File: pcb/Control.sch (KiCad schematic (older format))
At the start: 26 parts, among them P201 USB_OTG, P202 CONN_01X04, P203 CONN_01X04, U201 AP2114H, U202 STM32F072CBU

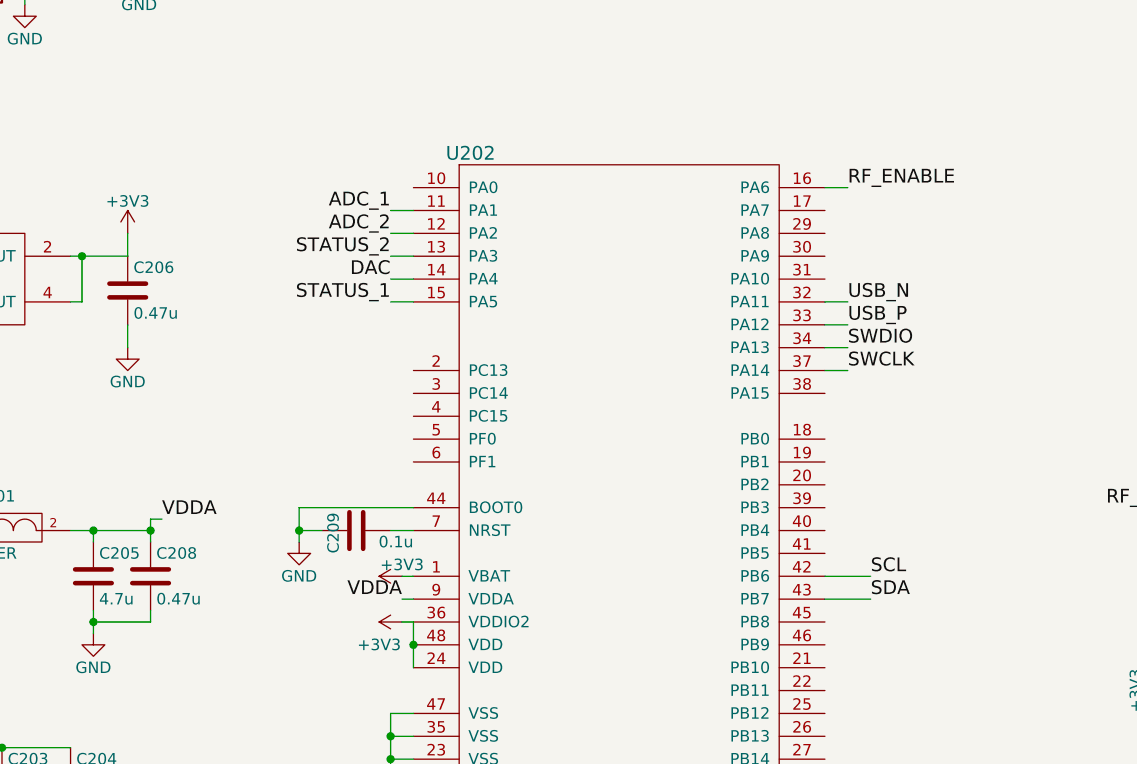
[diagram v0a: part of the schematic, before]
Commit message: finished PCB routing, begin design review
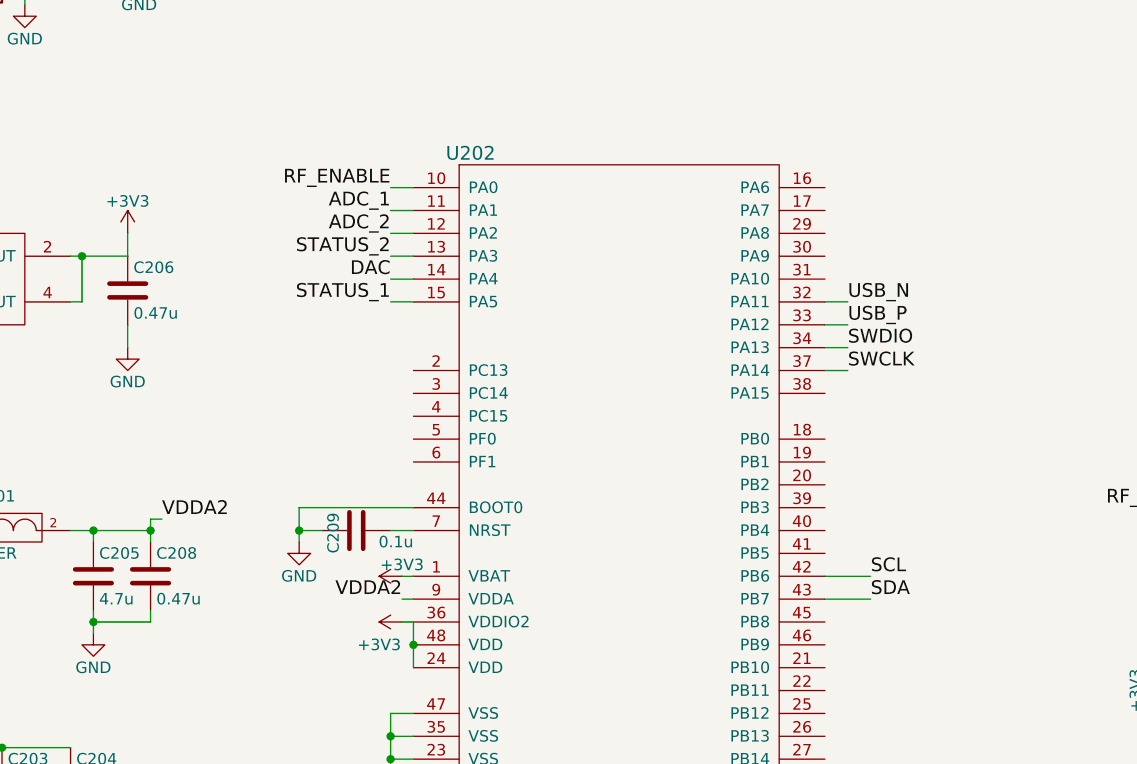
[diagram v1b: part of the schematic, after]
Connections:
- net RF_ENABLE: now also U202.10 (PA0); no longer U202.16 (PA6)
- net VDDA renamed VDDA2
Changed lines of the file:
@@
 $EndComp
 Text Label 3350 4100 2    60   ~ 0
-VDDA
+VDDA2
 $Comp
 L FILTER FB201
@@
 $EndComp
 Text Label 2300 3750 0    60   ~ 0
-VDDA
+VDDA2
 Text Notes 1450 5250 0    60   ~ 0
 VDD Decoupling
-Text Label 5300 2300 0    60   ~ 0
+Text Label 3300 2300 2    60   ~ 0
 RF_ENABLE
 Text Label 6900 3400 2    60   ~ 0
@@
 Connection ~ 2250 3800
 Wire Wire Line
-	5200 2300 5300 2300
+	3400 2300 3300 2300
 Wire Wire Line
 	6900 3400 7300 3400

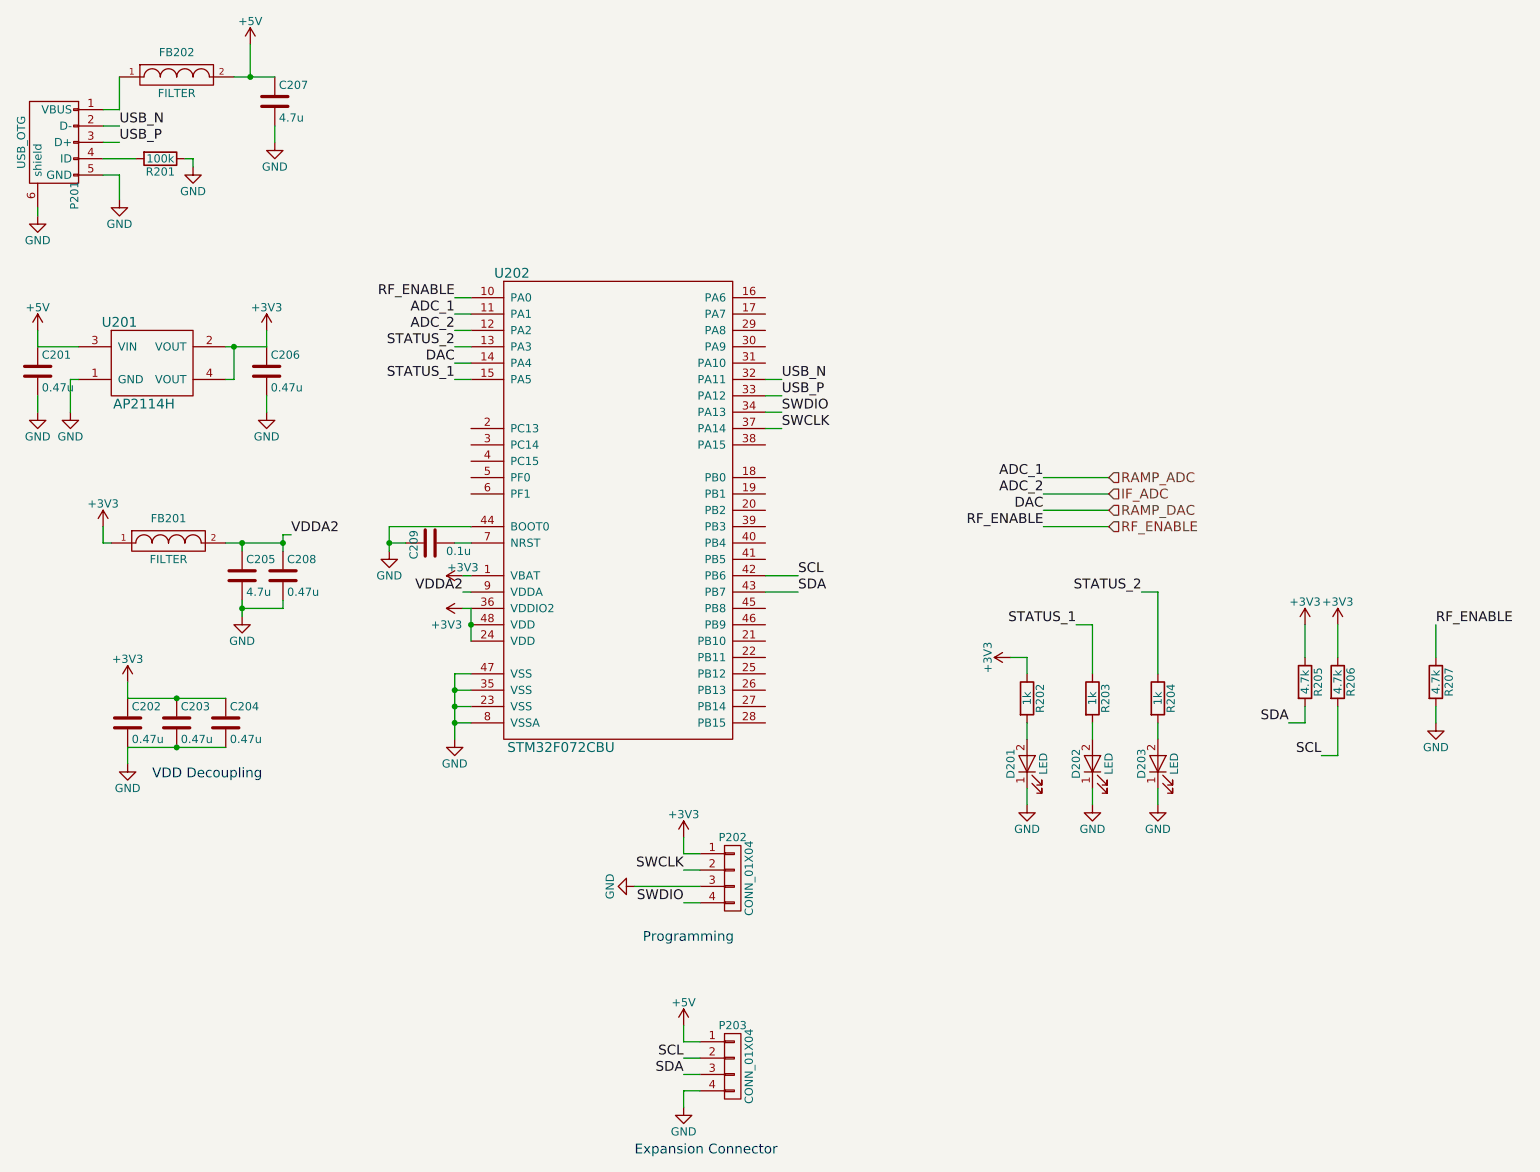
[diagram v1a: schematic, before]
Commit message: new uc and added AGC. Sent off to fab
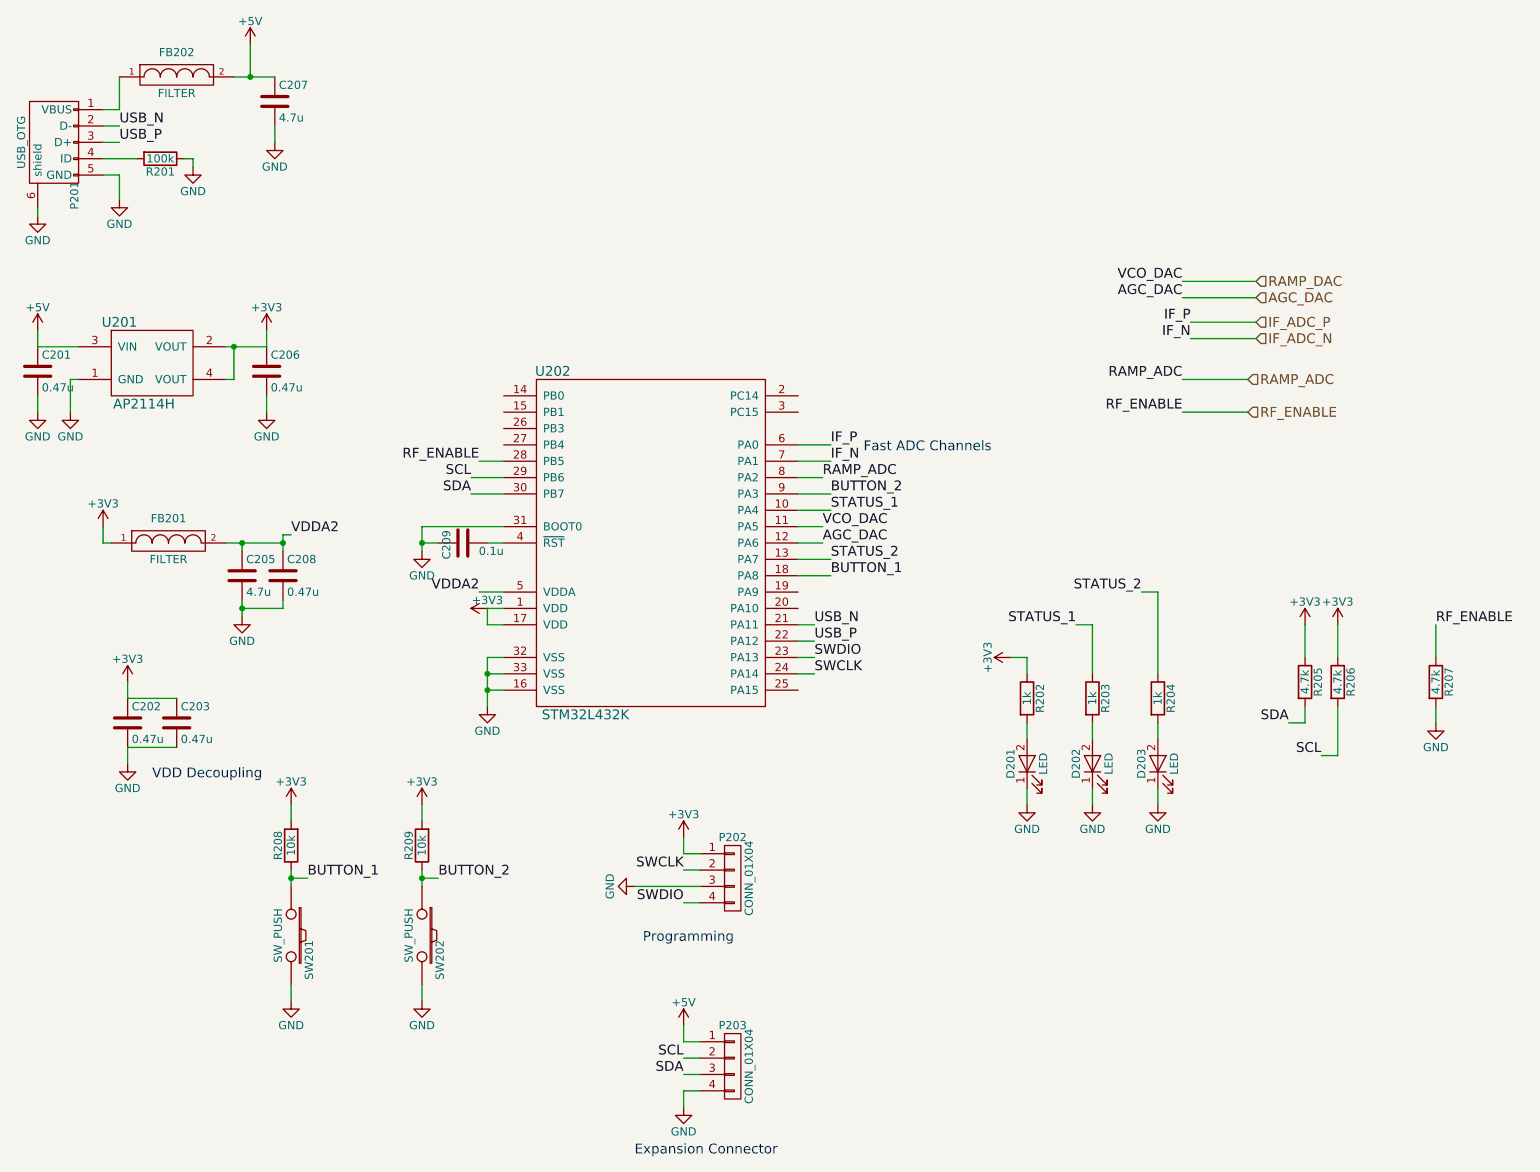
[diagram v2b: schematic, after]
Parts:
- removed C204: 0.47u, Capacitors_SMD:C_0603, symbol C
- removed U202: STM32F072CBU, Housings_DFN_QFN:QFN-48-1EP_7x7mm_Pitch0.5mm, symbol STM32F072CBU
- added R208, R209: 10k, Resistors_SMD:R_0603, symbol R
- added SW201, SW202: SW_PUSH, wbraun_smd:button-5mm, symbol SW_PUSH
- added U202: STM32L432K, Housings_DFN_QFN:QFN-32-1EP_5x5mm_Pitch0.5mm, symbol STM32L432K
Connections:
- net +3V3: now also R208.2, R209.2, U202.1 (VDD), U202.17 (VDD)
- net GND: now also SW201.2, SW202.2, U202.16 (VSS), U202.31 (BOOT0), U202.32 (VSS), U202.33 (VSS)
- net RAMP_ADC: now also U202.8 (PA2)
- net RAMP_DAC: now also U202.11 (PA5)
- net RF_ENABLE: now also U202.28 (PB5)
- net SCL: now also U202.29 (PB6)
- net SDA: now also U202.30 (PB7)
- net STATUS_1: now also U202.10 (PA4)
- net STATUS_2: now also U202.13 (PA7)
- net SWCLK: now also U202.24 (PA14)
- net SWDIO: now also U202.23 (PA13)
- net USB_N: now also U202.21 (PA11)
- net USB_P: now also U202.22 (PA12)
- net VDDA2: now also U202.5 (VDDA)
- net at C209.2: now also U202.4 (~RST~)
- new net AGC_DAC: U202.12 (PA6)
- new net BUTTON_1: R208.1, SW201.1, U202.18 (PA8)
- new net BUTTON_2: R209.1, SW202.1, U202.9 (PA3)
- new net IF_ADC_N: U202.7 (PA1)
- new net IF_ADC_P: U202.6 (PA0)
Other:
- note added: "Fast ADC Channels"
- moved on the sheet: C209

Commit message: fixed DAC pin swap on radar board
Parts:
- P201: symbol USB_OTG -> USB_OTG-RESCUE-tiny-radar
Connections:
- net AGC_DAC: now also U202.10 (PA4); no longer U202.12 (PA6)
- net STATUS_1: now also U202.12 (PA6); no longer U202.10 (PA4)
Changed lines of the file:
@@
 EESchema Schematic File Version 2
+LIBS:tiny-radar-rescue
 LIBS:power
 LIBS:device
@@
 $EndDescr
 $Comp
-L USB_OTG P201
+L USB_OTG-RESCUE-tiny-radar P201
 U 1 1 58AAD76F
 P 850 1350
+AR Path="/58AAD76F" Ref="P201"  Part="1"
+AR Path="/58AA0025/58AAD76F" Ref="P201"  Part="1"
 F 0 "P201" H 1175 1225 50  0000 C CNN
 F 1 "USB_OTG" H 850 1550 50  0000 C CNN
@@
 Text Label 5550 3700 0    60   ~ 0
 VCO_DAC
-Text Label 5550 3800 0    60   ~ 0
+Text Label 5600 3600 0    60   ~ 0
 AGC_DAC
 Text Label 5550 3400 0    60   ~ 0
@@
 	1    0    0    -1
 $EndComp
-Text Label 5600 3600 0    60   ~ 0
+Text Label 5550 3800 0    60   ~ 0
 STATUS_1
 Text Label 5600 3900 0    60   ~ 0
